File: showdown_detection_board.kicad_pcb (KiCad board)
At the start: 2 copper layers, 31 parts, among them J1 Conn_01x04_Pin, J2 USB4155-03-C_REVA, SW1 SW_SPDT, U1 AMS1117-3.3, U2 MCP6002-xMC, U3 STM32F103C8T6, Y1 16MHz

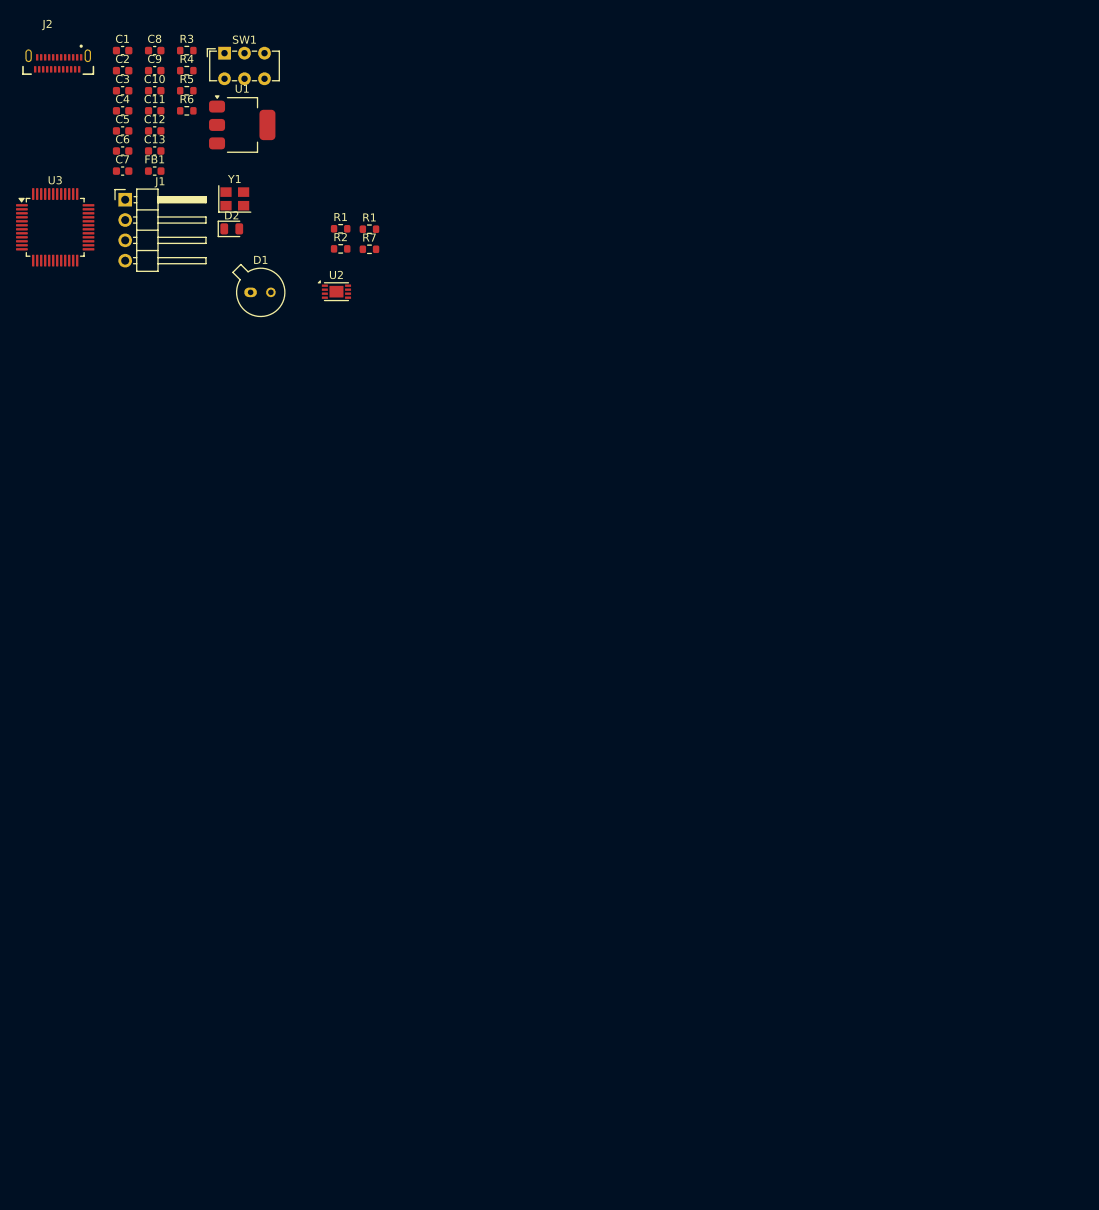
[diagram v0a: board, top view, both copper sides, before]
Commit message: most of schematic is complete
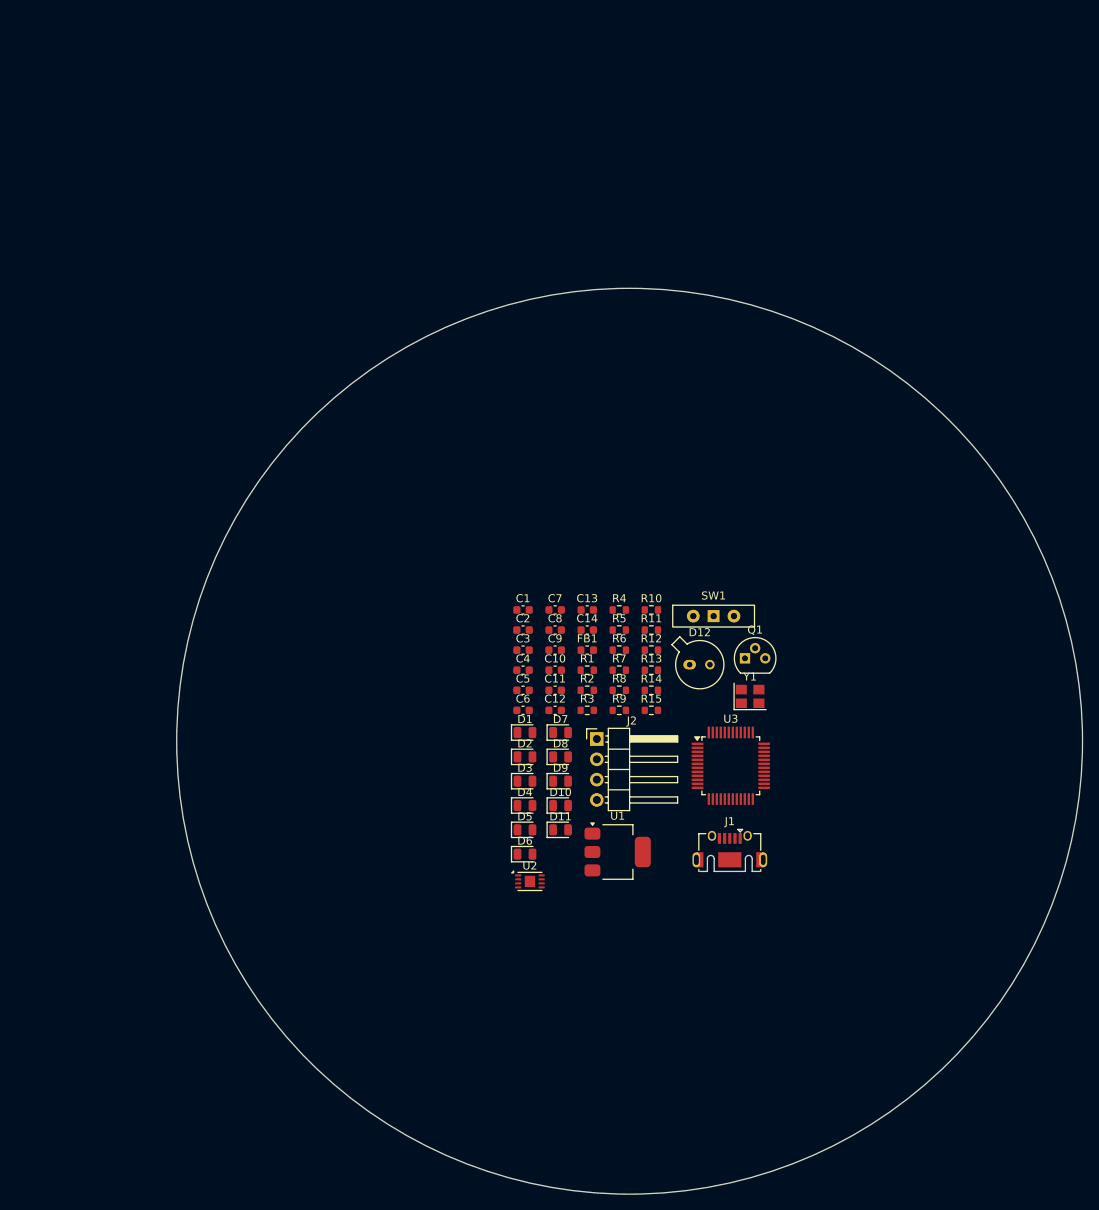
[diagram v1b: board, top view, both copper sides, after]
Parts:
- removed the R1 at (177.1, 84.4)
- removed the R1 at (180.7, 84.4)
- added C14: 1uF, Capacitor_SMD:C_0603_1608Metric, F.Cu at (207.9, 134.5)
- added D10: LED_BLUE, LED_SMD:LED_0805_2012Metric, F.Cu at (204.6, 156.5)
- added D11: LED_BLUE, LED_SMD:LED_0805_2012Metric, F.Cu at (204.6, 159.5)
- added D12: BPX65, Package_TO_SOT_THT:TO-18-2_Lens, F.Cu at (220.7, 138.9)
- added D3: LED_BLUE, LED_SMD:LED_0805_2012Metric, F.Cu at (200.2, 153.4)
- added D4: LED_BLUE, LED_SMD:LED_0805_2012Metric, F.Cu at (200.2, 156.5)
- added D5: LED_BLUE, LED_SMD:LED_0805_2012Metric, F.Cu at (200.2, 159.5)
- added D6: LED_BLUE, LED_SMD:LED_0805_2012Metric, F.Cu at (200.2, 162.6)
- added D7: LED_BLUE, LED_SMD:LED_0805_2012Metric, F.Cu at (204.6, 147.4)
- added D8: LED_BLUE, LED_SMD:LED_0805_2012Metric, F.Cu at (204.6, 150.4)
- added D9: LED_BLUE, LED_SMD:LED_0805_2012Metric, F.Cu at (204.6, 153.4)
- added Q1: 2N2222, Package_TO_SOT_THT:TO-92, F.Cu at (227.7, 138.1)
- added R1: 1K, Resistor_SMD:R_0603_1608Metric, F.Cu at (207.9, 139.6)
- added R10: 15R, Resistor_SMD:R_0603_1608Metric, F.Cu at (216.0, 132.0)
- added R11: 15R, Resistor_SMD:R_0603_1608Metric, F.Cu at (216.0, 134.5)
- added R12: 1.5K, Resistor_SMD:R_0603_1608Metric, F.Cu at (216.0, 137.1)
- added R13: 10K, Resistor_SMD:R_0603_1608Metric, F.Cu at (216.0, 139.6)
- added R14: 1M, Resistor_SMD:R_0603_1608Metric, F.Cu at (216.0, 142.1)
- added R15: 1.5K, Resistor_SMD:R_0603_1608Metric, F.Cu at (216.0, 144.6)
- added R8: 15R, Resistor_SMD:R_0603_1608Metric, F.Cu at (212.0, 142.1)
- added R9: 15R, Resistor_SMD:R_0603_1608Metric, F.Cu at (212.0, 144.6)
- C11: value 10nF -> 100nF
- C12: value 1uF -> 10nF
- C9: value 100nF -> 10uF
- D1: value BPX65 -> LED_RED; footprint Package_TO_SOT_THT:TO-18-2_Lens -> LED_SMD:LED_0805_2012Metric
- D2: value LED_RED -> LED_BLUE
- J1: value Conn_01x04_Pin -> USB_B_Micro; footprint Connector_PinHeader_2.54mm:PinHeader_1x04_P2.54mm_Horizontal -> Connector_USB:USB_Micro-AB_Molex_47590-0001
- J2: value USB4155-03-C_REVA -> Conn_01x04_Pin; footprint USB4155-03-C_REVA:GCT_USB4155-03-C_REVA -> Connector_PinHeader_2.54mm:PinHeader_1x04_P2.54mm_Horizontal
- R2, R3, R5: value 1.5K -> 15R
- R4: value 10K -> 15R
- R6: value 5.1K -> 15R
- R7: value 1M -> 15R
- SW1: footprint Button_Switch_THT:SW_E-Switch_EG1271_SPDT -> Button_Switch_THT:SW_Slide-03_Wuerth-WS-SLTV_10x2.5x6.4_P2.54mm
- U2: value MCP6002-xMC -> MCP6002; footprint Package_DFN_QFN:DFN-8-1EP_3x2mm_P0.5mm_EP1.75x1.45mm -> Package_DFN_QFN:TDFN-8-1EP_3x2mm_P0.5mm_EP1.3x1.4mm
- moved J1 111.9 mm to (225.8, 163.3)
- moved J2 108.0 mm to (209.1, 148.2)
- moved U3 108.0 mm to (225.9, 151.5)
- moved U1 102.3 mm to (211.7, 162.3)
- moved R3 96.5 mm to (207.9, 144.6)
- moved SW1 93.2 mm to (223.7, 132.8)
- moved Y1 89.5 mm to (228.3, 142.8)
- moved C11 88.0 mm to (203.9, 142.1)
- moved C10 88.0 mm to (203.9, 139.6)
- moved C12 88.0 mm to (203.9, 144.6)
- moved C8 88.0 mm to (203.9, 134.5)
- moved C9 88.0 mm to (203.9, 137.1)
- moved R5 86.4 mm to (212.0, 134.5)
- moved R6 86.4 mm to (212.0, 137.1)
- moved R4 86.4 mm to (212.0, 132.0)
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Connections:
- C11 pad 1: +3V3_A -> +3V3
- C13 pad 1: +3V3 -> +3V3_A
- C9 pad 1: +3V3 -> /hit_register
- C9 pad 2: GND -> Net-(D12-K)
- D1 pad 1: Net-(D1-K) -> /PWR_LED_K
- D1 pad 2: GND -> +3V3
- D2 pad 1: /PWR_LED_K -> Net-(D2-K)
- J1 pad 1: +3V3 -> VBUS
- J1 pad 2: /SWDIO -> /USB_D-
- J1 pad 3: /SWCLK -> /USB_D+
- J1 pad 4: GND -> unconnected-(J1-ID-Pad4)
- R2 pad 1: Net-(U2A--) -> Net-(D2-K)
- R2 pad 2: GND -> Net-(Q1-C)
- R3 pad 1: GND -> Net-(D3-K)
- R3 pad 2: /PWR_LED_K -> Net-(Q1-C)
- R4 pad 1: /SW_BOOT0 -> Net-(D4-K)
- R4 pad 2: /BOOT0 -> Net-(Q1-C)
- R5 pad 1: /USB_D+ -> Net-(D5-K)
- R5 pad 2: +3V3 -> Net-(Q1-C)
- R6 pad 1: GND -> Net-(D6-K)
- R6 pad 2: Net-(J2-CC1) -> Net-(Q1-C)
- R7 pad 1: /hit_register -> Net-(D7-K)
- R7 pad 2: Net-(D1-K) -> Net-(Q1-C)
- U2 pad 1: /hit_register -> GND
- U2 pad 2: Net-(U2A--) -> Net-(D12-K)
- U2 pad 3: Net-(D1-K) -> +3V3
- U2 pad 4: (no net) -> GND
- U2 pad 5: (no net) -> /hit_register
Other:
- board outline added: 113.2 x 113.2 mm

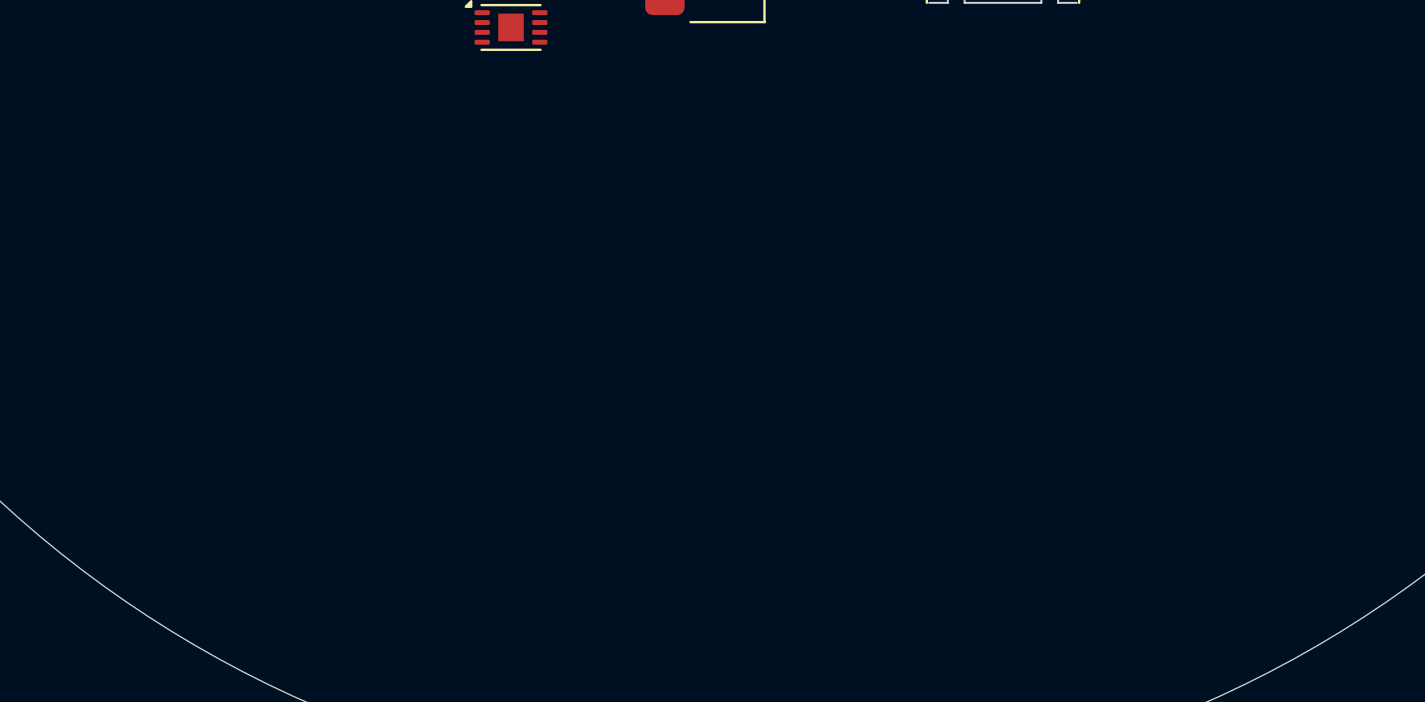
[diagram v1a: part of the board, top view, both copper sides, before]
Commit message: started working on battery cir.
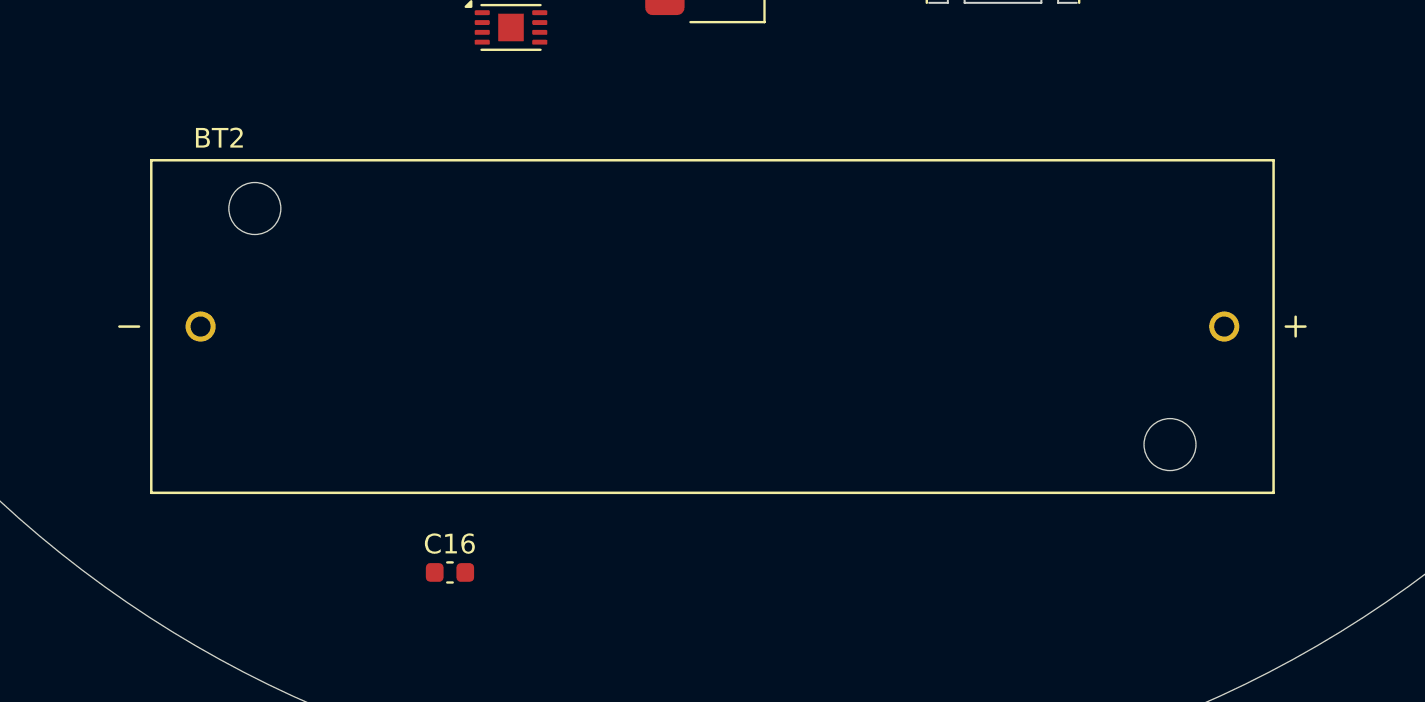
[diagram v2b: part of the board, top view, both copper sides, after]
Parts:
- added BT2: 2460, 2460:BAT_2460, F.Cu at (211.0, 181.2)
- added C16: 10uF, Capacitor_SMD:C_0603_1608Metric, F.Cu at (197.7, 193.7)
